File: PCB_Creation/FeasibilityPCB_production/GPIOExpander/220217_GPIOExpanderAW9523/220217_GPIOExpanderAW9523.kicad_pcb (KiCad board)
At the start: 2 copper layers, 100 x 65 mm, 57 parts, among them IC1 AW9523BTQR, J1 PWR_Bottom1, J2 PWR_Bottom2, J3 P0_0-07, J4 P0_0-07, J5 I2C ComPort, J6 PWR_Top, J7 Conn_02x08_Odd_Even, J8 Conn_01x08_Male, J9 Conn_01x08_Male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

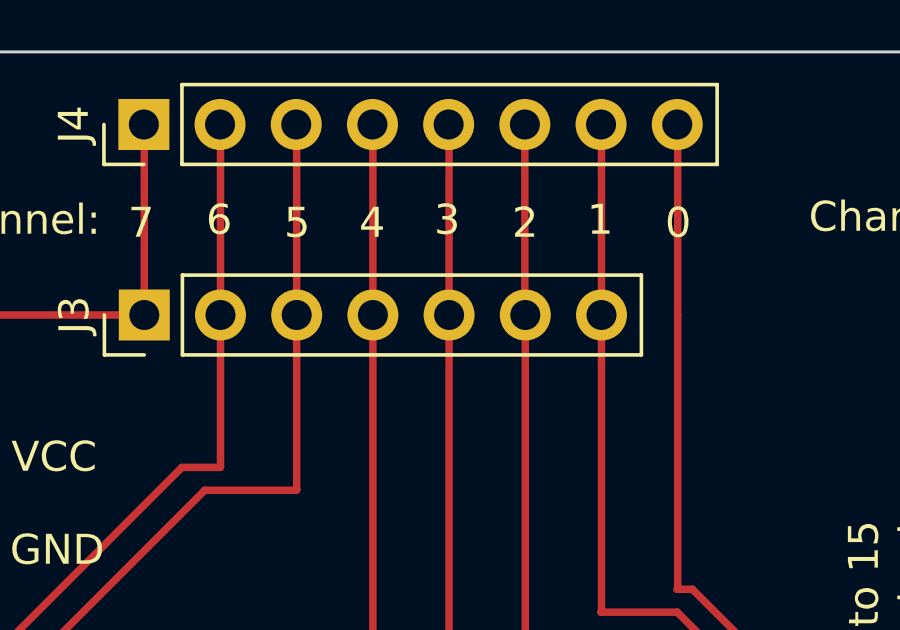
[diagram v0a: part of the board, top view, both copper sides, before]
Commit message: MCU Folder Added
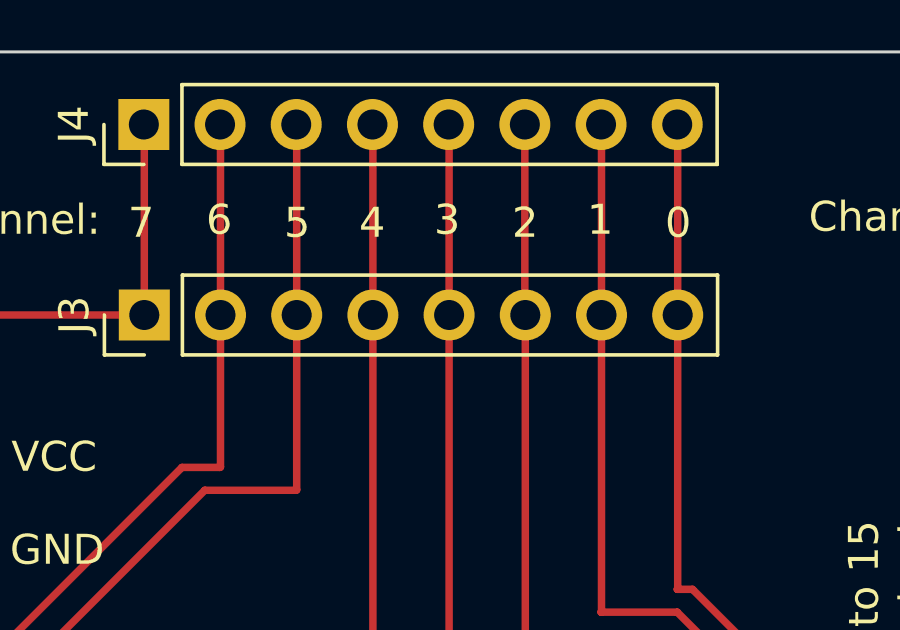
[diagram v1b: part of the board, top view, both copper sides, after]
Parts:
- D6: value White -> Orange
- J3: footprint Connector_PinHeader_2.54mm:PinHeader_1x07_P2.54mm_Vertical -> Connector_PinHeader_2.54mm:PinHeader_1x08_P2.54mm_Vertical
